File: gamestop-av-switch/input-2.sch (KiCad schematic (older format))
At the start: 8 parts

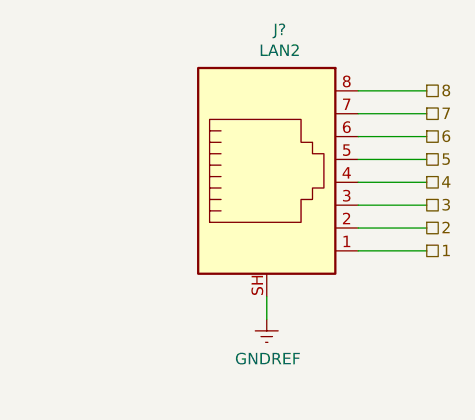
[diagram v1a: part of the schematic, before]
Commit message: Cleaning up extra ethernet pins
Setting no connects on the ports themselves and eliminating the extra
heirarchal labels and pins
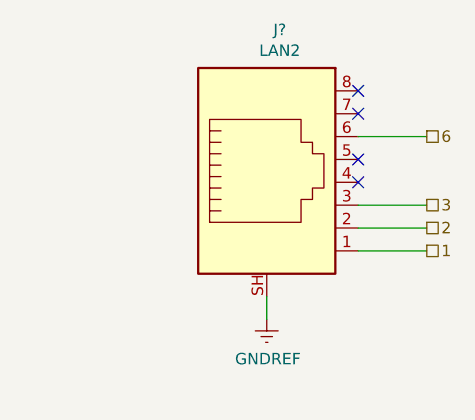
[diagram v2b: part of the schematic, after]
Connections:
- net 4: no longer names the net of J?.4
- net 5: no longer names the net of J?.5
- net 7: no longer names the net of J?.7
- net 8: no longer names the net of J?.8
- no-connect marks 0 -> 4
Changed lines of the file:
@@
 Text HLabel 9900 3350 2    50   UnSpc ~ 0
 3
-Text HLabel 9900 3250 2    50   UnSpc ~ 0
-4
-Text HLabel 9900 3150 2    50   UnSpc ~ 0
-5
 Text HLabel 9900 3050 2    50   UnSpc ~ 0
 6
-Text HLabel 9900 2950 2    50   UnSpc ~ 0
-7
-Text HLabel 9900 2850 2    50   UnSpc ~ 0
-8
-Wire Wire Line
-	9600 2850 9900 2850
-Wire Wire Line
-	9600 2950 9900 2950
 Wire Wire Line
 	9600 3050 9900 3050
-Wire Wire Line
-	9600 3150 9900 3150
-Wire Wire Line
-	9600 3250 9900 3250
 Wire Wire Line
 	9600 3350 9900 3350
@@
 Wire Wire Line
 	9200 3850 9200 3750
+NoConn ~ 9600 2850
+NoConn ~ 9600 2950
+NoConn ~ 9600 3150
+NoConn ~ 9600 3250
 $EndSCHEMATC

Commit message: Annotating and satisfying ERC
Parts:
- gave numbers to parts that had none: 8
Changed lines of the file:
@@
 AR Path="/60F9A3F1" Ref="J?"  Part="1"
 AR Path="/60F3FEDE/60F9A3F1" Ref="J?"  Part="1"
-AR Path="/60F422FE/60F9A3F1" Ref="J?"  Part="1"
+AR Path="/60F422FE/60F9A3F1" Ref="J82"  Part="1"
 AR Path="/60F4248B/60F9A3F1" Ref="J?"  Part="1"
-F 0 "J?" H 4900 3125 50  0000 L CNN
+F 0 "J82" H 4900 3125 50  0000 L CNN
 F 1 "RD2" H 4900 3034 50  0000 L CNN
 F 2 "" H 4800 3150 50  0001 C CNN
@@
 AR Path="/60F9A3F7" Ref="J?"  Part="1"
 AR Path="/60F3FEDE/60F9A3F7" Ref="J?"  Part="1"
-AR Path="/60F422FE/60F9A3F7" Ref="J?"  Part="1"
+AR Path="/60F422FE/60F9A3F7" Ref="J84"  Part="1"
 AR Path="/60F4248B/60F9A3F7" Ref="J?"  Part="1"
-F 0 "J?" H 7200 3767 50  0000 C CNN
+F 0 "J84" H 7200 3767 50  0000 C CNN
 F 1 "SV2" H 7200 3676 50  0000 C CNN
 F 2 "" H 7200 3400 50  0001 C CNN
@@
 AR Path="/60F9A3FD" Ref="J?"  Part="1"
 AR Path="/60F3FEDE/60F9A3FD" Ref="J?"  Part="1"
-AR Path="/60F422FE/60F9A3FD" Ref="J?"  Part="1"
+AR Path="/60F422FE/60F9A3FD" Ref="J85"  Part="1"
 AR Path="/60F4248B/60F9A3FD" Ref="J?"  Part="1"
-F 0 "J?" H 9257 3917 50  0000 C CNN
+F 0 "J85" H 9257 3917 50  0000 C CNN
 F 1 "LAN2" H 9257 3826 50  0000 C CNN
 F 2 "" V 9200 3275 50  0001 C CNN
@@
 AR Path="/60F9A403" Ref="J?"  Part="1"
 AR Path="/60F3FEDE/60F9A403" Ref="J?"  Part="1"
-AR Path="/60F422FE/60F9A403" Ref="J?"  Part="1"
+AR Path="/60F422FE/60F9A403" Ref="J83"  Part="1"
 AR Path="/60F4248B/60F9A403" Ref="J?"  Part="1"
-F 0 "J?" H 4900 3575 50  0000 L CNN
+F 0 "J83" H 4900 3575 50  0000 L CNN
 F 1 "G2" H 4900 3484 50  0000 L CNN
 F 2 "" H 4800 3600 50  0001 C CNN
@@
 AR Path="/60F9A409" Ref="J?"  Part="1"
 AR Path="/60F3FEDE/60F9A409" Ref="J?"  Part="1"
-AR Path="/60F422FE/60F9A409" Ref="J?"  Part="1"
+AR Path="/60F422FE/60F9A409" Ref="J80"  Part="1"
 AR Path="/60F4248B/60F9A409" Ref="J?"  Part="1"
-F 0 "J?" H 3650 3125 50  0000 L CNN
+F 0 "J80" H 3650 3125 50  0000 L CNN
 F 1 "B2" H 3650 3034 50  0000 L CNN
 F 2 "" H 3550 3150 50  0001 C CNN
@@
 AR Path="/60F9A40F" Ref="J?"  Part="1"
 AR Path="/60F3FEDE/60F9A40F" Ref="J?"  Part="1"
-AR Path="/60F422FE/60F9A40F" Ref="J?"  Part="1"
+AR Path="/60F422FE/60F9A40F" Ref="J81"  Part="1"
 AR Path="/60F4248B/60F9A40F" Ref="J?"  Part="1"
-F 0 "J?" H 3650 3575 50  0000 L CNN
+F 0 "J81" H 3650 3575 50  0000 L CNN
 F 1 "Y2" H 3650 3484 50  0000 L CNN
 F 2 "" H 3550 3600 50  0001 C CNN
@@
 AR Path="/60F9A415" Ref="J?"  Part="1"
 AR Path="/60F3FEDE/60F9A415" Ref="J?"  Part="1"
-AR Path="/60F422FE/60F9A415" Ref="J?"  Part="1"
+AR Path="/60F422FE/60F9A415" Ref="J78"  Part="1"
 AR Path="/60F4248B/60F9A415" Ref="J?"  Part="1"
-F 0 "J?" H 2550 3125 50  0000 L CNN
+F 0 "J78" H 2550 3125 50  0000 L CNN
 F 1 "R2" H 2550 3034 50  0000 L CNN
 F 2 "" H 2450 3150 50  0001 C CNN
@@
 AR Path="/60F9A41B" Ref="J?"  Part="1"
 AR Path="/60F3FEDE/60F9A41B" Ref="J?"  Part="1"
-AR Path="/60F422FE/60F9A41B" Ref="J?"  Part="1"
+AR Path="/60F422FE/60F9A41B" Ref="J79"  Part="1"
 AR Path="/60F4248B/60F9A41B" Ref="J?"  Part="1"
-F 0 "J?" H 2550 3575 50  0000 L CNN
+F 0 "J79" H 2550 3575 50  0000 L CNN
 F 1 "L2" H 2550 3484 50  0000 L CNN
 F 2 "" H 2450 3600 50  0001 C CNN
@@
 C
 $Comp
-L power:GNDREF #PWR?
+L power:GNDREF #PWR05
 U 1 1 60F9A428
 P 5200 4100
-F 0 "#PWR?" H 5200 3850 50  0001 C CNN
+F 0 "#PWR05" H 5200 3850 50  0001 C CNN
 F 1 "GNDREF" H 5205 3927 50  0000 C CNN
 F 2 "" H 5200 4100 50  0001 C CNN
@@
 Connection ~ 7200 3800
 $Comp
-L power:GNDREF #PWR?
+L power:GNDREF #PWR06
 U 1 1 60F9A452
 P 6800 3950
-F 0 "#PWR?" H 6800 3700 50  0001 C CNN
+F 0 "#PWR06" H 6800 3700 50  0001 C CNN
 F 1 "GNDREF" H 6805 3777 50  0000 C CNN
 F 2 "" H 6800 3950 50  0001 C CNN
@@
 	9600 3550 9900 3550
 $Comp
-L power:GNDREF #PWR?
+L power:GNDREF #PWR07
 U 1 1 60F9A46A
 P 9200 3850
-F 0 "#PWR?" H 9200 3600 50  0001 C CNN
+F 0 "#PWR07" H 9200 3600 50  0001 C CNN
 F 1 "GNDREF" H 9205 3677 50  0000 C CNN
 F 2 "" H 9200 3850 50  0001 C CNN
